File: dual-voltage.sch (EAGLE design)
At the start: 14 parts

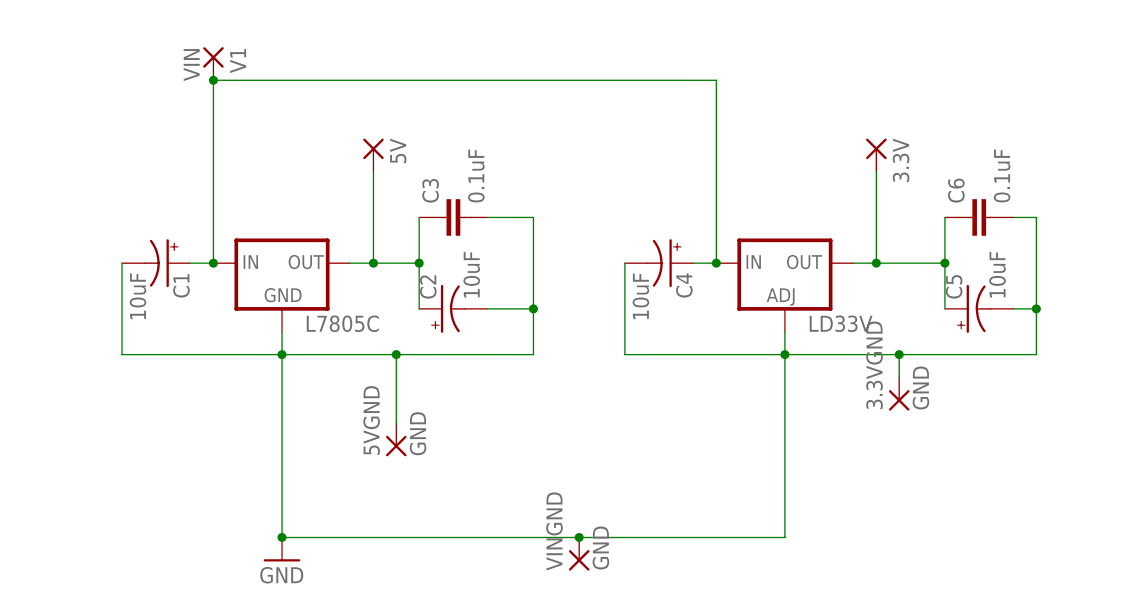
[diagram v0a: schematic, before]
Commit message: Trace updates for new 3.3v regulator
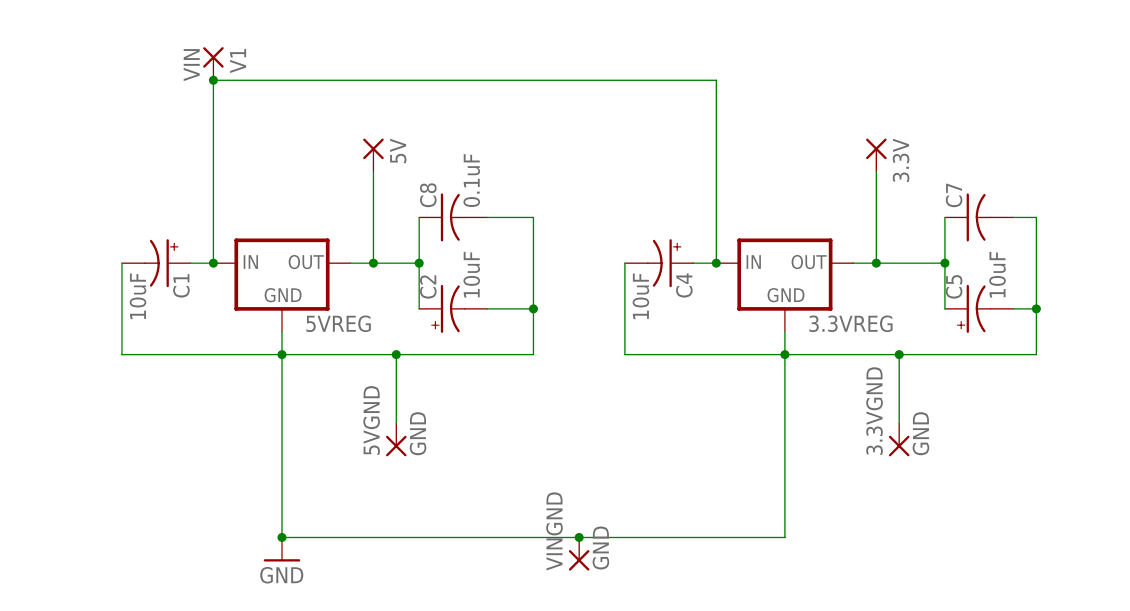
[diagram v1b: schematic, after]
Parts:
- removed C3, C6: 0.1uF, SparkFun-Capacitors:CAPEZ
- removed LD33V: (no value), v-reg:LM317TS
- added 3.3VREG: (no value), v-reg:78XXS
- added C7: (no value), rcl:C-US025-025X050
- added C8: 0.1uF, rcl:C-US025-025X050
- renumbered L7805C to 5VREG
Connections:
- net 3.3V: now also 3.3VREG.OUT, C7.1; no longer C6.1, LD33V.OUT
- net 5V: now also C8.1; no longer C3.1
- net GND: now also 3.3VREG.GND, C7.2, C8.2; no longer C3.2, C6.2, LD33V.ADJ
- net N$1: now also 3.3VREG.IN; no longer LD33V.IN
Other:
- moved on the sheet: 3.3VGND
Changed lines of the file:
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@@
 <part name="C5" library="SparkFun-Capacitors" deviceset="CAP_POL" device="PTH2" value="10uF"/>
 <part name="C4" library="SparkFun-Capacitors" deviceset="CAP_POL" device="PTH2" value="10uF"/>
-<part name="C3" library="SparkFun-Capacitors" deviceset="CAP" device="EZ" value="0.1uF"/>
-<part name="C6" library="SparkFun-Capacitors" deviceset="CAP" device="EZ" value="0.1uF"/>
-<part name="LD33V" library="v-reg" deviceset="LM317TS" device=""/>
-<part name="L7805C" library="v-reg" deviceset="78XXS" device=""/>
+<part name="5VREG" library="v-reg" deviceset="78XXS" device=""/>
 <part name="5V" library="wirepad" deviceset="1,6/0,8" device=""/>
 <part name="3.3V" library="wirepad" deviceset="1,6/0,8" device=""/>
@@
 <part name="VINGND" library="wirepad" deviceset="1,6/0,8" device="" value="GND"/>
 <part name="GND1" library="supply1" deviceset="GND" device=""/>
+<part name="3.3VREG" library="v-reg" deviceset="78XXS" device=""/>
+<part name="C7" library="rcl" deviceset="C-US" device="025-025X050"/>
+<part name="C8" library="rcl" deviceset="C-US" device="025-025X050" value="0.1uF"/>
 </parts>
 <sheets>
@@
 <instance part="C5" gate="G$1" x="109.22" y="53.34" rot="R90"/>
 <instance part="C4" gate="G$1" x="76.2" y="58.42" rot="R270"/>
-<instance part="C3" gate="G$1" x="53.34" y="63.5" rot="R90"/>
-<instance part="C6" gate="G$1" x="111.76" y="63.5" rot="R90"/>
-<instance part="LD33V" gate="1" x="88.9" y="58.42"/>
-<instance part="L7805C" gate="1" x="33.02" y="58.42"/>
+<instance part="5VREG" gate="1" x="33.02" y="58.42"/>
 <instance part="5V" gate="P" x="43.18" y="71.12" rot="R270"/>
 <instance part="3.3V" gate="P" x="99.06" y="71.12" rot="R270"/>
-<instance part="3.3VGND" gate="P" x="101.6" y="43.18" rot="R90"/>
+<instance part="3.3VGND" gate="P" x="101.6" y="38.1" rot="R90"/>
 <instance part="5VGND" gate="P" x="45.72" y="38.1" rot="R90"/>
 <instance part="V1" gate="P" x="25.4" y="81.28" rot="R270"/>
 <instance part="VINGND" gate="P" x="66.04" y="25.4" rot="R90"/>
 <instance part="GND1" gate="1" x="33.02" y="25.4"/>
+<instance part="3.3VREG" gate="1" x="88.9" y="58.42"/>
+<instance part="C7" gate="G$1" x="109.22" y="63.5" rot="R90"/>
+<instance part="C8" gate="G$1" x="50.8" y="63.5" rot="R90"/>
 </instances>
 <busses>
@@
 <net name="5V" class="0">
 <segment>
-<pinref part="C3" gate="G$1" pin="1"/>
 <wire x1="40.64" y1="58.42" x2="43.18" y2="58.42" width="0.1524" layer="91"/>
 <wire x1="43.18" y1="58.42" x2="48.26" y2="58.42" width="0.1524" layer="91"/>
@@
 <wire x1="48.26" y1="53.34" x2="48.26" y2="58.42" width="0.1524" layer="91"/>
 <junction x="48.26" y="58.42"/>
-<pinref part="L7805C" gate="1" pin="OUT"/>
+<pinref part="5VREG" gate="1" pin="OUT"/>
 <pinref part="5V" gate="P" pin="P"/>
 <wire x1="43.18" y1="68.58" x2="43.18" y2="58.42" width="0.1524" layer="91"/>
 <junction x="43.18" y="58.42"/>
+<pinref part="C8" gate="G$1" pin="1"/>
 </segment>
 </net>
 <net name="3.3V" class="0">
 <segment>
-<pinref part="C6" gate="G$1" pin="1"/>
 <wire x1="96.52" y1="58.42" x2="99.06" y2="58.42" width="0.1524" layer="91"/>
 <wire x1="99.06" y1="58.42" x2="106.68" y2="58.42" width="0.1524" layer="91"/>
@@
 <junction x="106.68" y="58.42"/>
 <junction x="99.06" y="58.42"/>
-<pinref part="LD33V" gate="1" pin="OUT"/>
 <pinref part="3.3V" gate="P" pin="P"/>
 <wire x1="99.06" y1="68.58" x2="99.06" y2="58.42" width="0.1524" layer="91"/>
+<pinref part="3.3VREG" gate="1" pin="OUT"/>
+<pinref part="C7" gate="G$1" pin="1"/>
 </segment>
 </net>
@@
 <wire x1="22.86" y1="58.42" x2="25.4" y2="58.42" width="0.1524" layer="91"/>
 <wire x1="25.4" y1="78.74" x2="25.4" y2="58.42" width="0.1524" layer="91"/>
-<pinref part="L7805C" gate="1" pin="IN"/>
+<pinref part="5VREG" gate="1" pin="IN"/>
 <junction x="25.4" y="58.42"/>
 <pinref part="V1" gate="P" pin="P"/>
 <pinref part="C4" gate="G$1" pin="+"/>
 <wire x1="78.74" y1="58.42" x2="81.28" y2="58.42" width="0.1524" layer="91"/>
-<pinref part="LD33V" gate="1" pin="IN"/>
 <wire x1="25.4" y1="78.74" x2="81.28" y2="78.74" width="0.1524" layer="91"/>
 <wire x1="81.28" y1="78.74" x2="81.28" y2="58.42" width="0.1524" layer="91"/>
 <junction x="25.4" y="78.74"/>
+<pinref part="3.3VREG" gate="1" pin="IN"/>
 <junction x="81.28" y="58.42"/>
 </segment>
@@
 <wire x1="60.96" y1="53.34" x2="60.96" y2="48.26" width="0.1524" layer="91"/>
 <wire x1="60.96" y1="48.26" x2="45.72" y2="48.26" width="0.1524" layer="91"/>
-<pinref part="C3" gate="G$1" pin="2"/>
 <wire x1="55.88" y1="63.5" x2="60.96" y2="63.5" width="0.1524" layer="91"/>
 <wire x1="60.96" y1="63.5" x2="60.96" y2="53.34" width="0.1524" layer="91"/>
@@
 <wire x1="71.12" y1="58.42" x2="71.12" y2="48.26" width="0.1524" layer="91"/>
 <wire x1="71.12" y1="48.26" x2="88.9" y2="48.26" width="0.1524" layer="91"/>
-<pinref part="C6" gate="G$1" pin="2"/>
 <wire x1="88.9" y1="48.26" x2="101.6" y2="48.26" width="0.1524" layer="91"/>
 <wire x1="114.3" y1="63.5" x2="116.84" y2="63.5" width="0.1524" layer="91"/>
@@
 <junction x="116.84" y="53.34"/>
 <pinref part="3.3VGND" gate="P" pin="P"/>
-<wire x1="101.6" y1="45.72" x2="101.6" y2="48.26" width="0.1524" layer="91"/>
+<wire x1="101.6" y1="40.64" x2="101.6" y2="48.26" width="0.1524" layer="91"/>
 <junction x="101.6" y="48.26"/>
 <wire x1="66.04" y1="27.94" x2="88.9" y2="27.94" width="0.1524" layer="91"/>
@@
 <pinref part="GND1" gate="1" pin="GND"/>
 <junction x="33.02" y="27.94"/>
+<pinref part="C8" gate="G$1" pin="2"/>
+<pinref part="C7" gate="G$1" pin="2"/>
 </segment>
 <segment>
-<pinref part="L7805C" gate="1" pin="GND"/>
+<pinref part="5VREG" gate="1" pin="GND"/>
 <wire x1="33.02" y1="50.8" x2="33.02" y2="48.26" width="0.1524" layer="91"/>
 </segment>
 <segment>
-<pinref part="LD33V" gate="1" pin="ADJ"/>
 <wire x1="88.9" y1="50.8" x2="88.9" y2="48.26" width="0.1524" layer="91"/>
+<pinref part="3.3VREG" gate="1" pin="GND"/>
 </segment>
 </net>

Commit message: Updates voltage in/out jumpers to SparkFun components, updates 0.1uF capacitor footprint to SparkFun, bumps version to 1.1.0
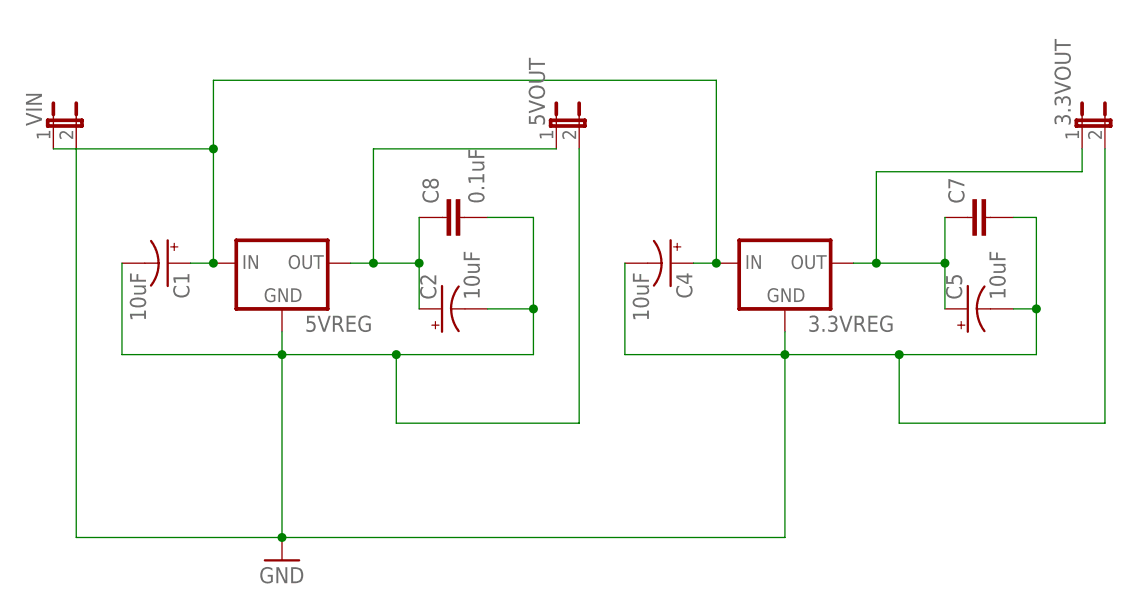
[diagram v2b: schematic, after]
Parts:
- removed 3.3V, 5V: (no value), wirepad:1,6/0,8
- removed 3.3VGND, 5VGND, VINGND: GND, wirepad:1,6/0,8
- removed V1: VIN, wirepad:1,6/0,8
- added 3.3VOUT, 5VOUT, VIN: (no value), SparkFun-Passives:JUMPER-2PTH
- C7, C8: device rcl:C-US025-025X050 -> SparkFun-Passives:CAPPTH2
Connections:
- net 3.3V: now also 3.3VOUT.1; no longer 3.3V.P
- net 5V: now also 5VOUT.1; no longer 5V.P
- net GND: now also 3.3VOUT.2, 5VOUT.2, VIN.2; no longer 3.3VGND.P, 5VGND.P, VINGND.P
- net N$1: now also VIN.1; no longer V1.P
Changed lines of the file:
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@@
 <part name="C4" library="SparkFun-Capacitors" deviceset="CAP_POL" device="PTH2" value="10uF"/>
 <part name="5VREG" library="v-reg" deviceset="78XXS" device=""/>
-<part name="5V" library="wirepad" deviceset="1,6/0,8" device=""/>
-<part name="3.3V" library="wirepad" deviceset="1,6/0,8" device=""/>
-<part name="3.3VGND" library="wirepad" deviceset="1,6/0,8" device="" value="GND"/>
-<part name="5VGND" library="wirepad" deviceset="1,6/0,8" device="" value="GND"/>
-<part name="V1" library="wirepad" deviceset="1,6/0,8" device="" value="VIN"/>
-<part name="VINGND" library="wirepad" deviceset="1,6/0,8" device="" value="GND"/>
 <part name="GND1" library="supply1" deviceset="GND" device=""/>
 <part name="3.3VREG" library="v-reg" deviceset="78XXS" device=""/>
-<part name="C7" library="rcl" deviceset="C-US" device="025-025X050"/>
-<part name="C8" library="rcl" deviceset="C-US" device="025-025X050" value="0.1uF"/>
+<part name="C7" library="SparkFun-Passives" deviceset="CAP" device="PTH2"/>
+<part name="C8" library="SparkFun-Passives" deviceset="CAP" device="PTH2" value="0.1uF"/>
+<part name="5VOUT" library="SparkFun-Passives" deviceset="JUMPER-2" device="PTH"/>
+<part name="3.3VOUT" library="SparkFun-Passives" deviceset="JUMPER-2" device="PTH"/>
+<part name="VIN" library="SparkFun-Passives" deviceset="JUMPER-2" device="PTH"/>
 </parts>
 <sheets>
@@
 <instance part="C4" gate="G$1" x="76.2" y="58.42" rot="R270"/>
 <instance part="5VREG" gate="1" x="33.02" y="58.42"/>
-<instance part="5V" gate="P" x="43.18" y="71.12" rot="R270"/>
-<instance part="3.3V" gate="P" x="99.06" y="71.12" rot="R270"/>
-<instance part="3.3VGND" gate="P" x="101.6" y="38.1" rot="R90"/>
-<instance part="5VGND" gate="P" x="45.72" y="38.1" rot="R90"/>
-<instance part="V1" gate="P" x="25.4" y="81.28" rot="R270"/>
-<instance part="VINGND" gate="P" x="66.04" y="25.4" rot="R90"/>
 <instance part="GND1" gate="1" x="33.02" y="25.4"/>
 <instance part="3.3VREG" gate="1" x="88.9" y="58.42"/>
-<instance part="C7" gate="G$1" x="109.22" y="63.5" rot="R90"/>
-<instance part="C8" gate="G$1" x="50.8" y="63.5" rot="R90"/>
+<instance part="C7" gate="G$1" x="111.76" y="63.5" rot="R90"/>
+<instance part="C8" gate="G$1" x="53.34" y="63.5" rot="R90"/>
+<instance part="5VOUT" gate="A" x="63.5" y="73.66"/>
+<instance part="3.3VOUT" gate="A" x="121.92" y="73.66"/>
+<instance part="VIN" gate="A" x="7.62" y="73.66"/>
 </instances>
 <busses>
@@
 <junction x="48.26" y="58.42"/>
 <pinref part="5VREG" gate="1" pin="OUT"/>
-<pinref part="5V" gate="P" pin="P"/>
-<wire x1="43.18" y1="68.58" x2="43.18" y2="58.42" width="0.1524" layer="91"/>
+<wire x1="43.18" y1="71.12" x2="43.18" y2="58.42" width="0.1524" layer="91"/>
 <junction x="43.18" y="58.42"/>
 <pinref part="C8" gate="G$1" pin="1"/>
+<pinref part="5VOUT" gate="A" pin="1"/>
+<wire x1="63.5" y1="71.12" x2="43.18" y2="71.12" width="0.1524" layer="91"/>
 </segment>
 </net>
@@
 <junction x="106.68" y="58.42"/>
 <junction x="99.06" y="58.42"/>
-<pinref part="3.3V" gate="P" pin="P"/>
 <wire x1="99.06" y1="68.58" x2="99.06" y2="58.42" width="0.1524" layer="91"/>
 <pinref part="3.3VREG" gate="1" pin="OUT"/>
 <pinref part="C7" gate="G$1" pin="1"/>
+<pinref part="3.3VOUT" gate="A" pin="1"/>
+<wire x1="99.06" y1="68.58" x2="121.92" y2="68.58" width="0.1524" layer="91"/>
+<wire x1="121.92" y1="68.58" x2="121.92" y2="71.12" width="0.1524" layer="91"/>
 </segment>
 </net>
@@
 <pinref part="C1" gate="G$1" pin="+"/>
 <wire x1="22.86" y1="58.42" x2="25.4" y2="58.42" width="0.1524" layer="91"/>
-<wire x1="25.4" y1="78.74" x2="25.4" y2="58.42" width="0.1524" layer="91"/>
+<wire x1="25.4" y1="78.74" x2="25.4" y2="71.12" width="0.1524" layer="91"/>
 <pinref part="5VREG" gate="1" pin="IN"/>
 <junction x="25.4" y="58.42"/>
-<pinref part="V1" gate="P" pin="P"/>
 <pinref part="C4" gate="G$1" pin="+"/>
+<wire x1="25.4" y1="71.12" x2="25.4" y2="58.42" width="0.1524" layer="91"/>
 <wire x1="78.74" y1="58.42" x2="81.28" y2="58.42" width="0.1524" layer="91"/>
 <wire x1="25.4" y1="78.74" x2="81.28" y2="78.74" width="0.1524" layer="91"/>
 <wire x1="81.28" y1="78.74" x2="81.28" y2="58.42" width="0.1524" layer="91"/>
-<junction x="25.4" y="78.74"/>
 <pinref part="3.3VREG" gate="1" pin="IN"/>
 <junction x="81.28" y="58.42"/>
+<pinref part="VIN" gate="A" pin="1"/>
+<wire x1="7.62" y1="71.12" x2="25.4" y2="71.12" width="0.1524" layer="91"/>
+<junction x="25.4" y="71.12"/>
 </segment>
 </net>
@@
 <wire x1="60.96" y1="63.5" x2="60.96" y2="53.34" width="0.1524" layer="91"/>
 <junction x="60.96" y="53.34"/>
-<pinref part="5VGND" gate="P" pin="P"/>
 <wire x1="45.72" y1="40.64" x2="45.72" y2="48.26" width="0.1524" layer="91"/>
 <junction x="45.72" y="48.26"/>
-<pinref part="VINGND" gate="P" pin="P"/>
-<wire x1="66.04" y1="27.94" x2="33.02" y2="27.94" width="0.1524" layer="91"/>
+<wire x1="88.9" y1="27.94" x2="33.02" y2="27.94" width="0.1524" layer="91"/>
 <wire x1="33.02" y1="27.94" x2="33.02" y2="48.26" width="0.1524" layer="91"/>
 <junction x="33.02" y="48.26"/>
@@
 <wire x1="114.3" y1="53.34" x2="116.84" y2="53.34" width="0.1524" layer="91"/>
 <junction x="116.84" y="53.34"/>
-<pinref part="3.3VGND" gate="P" pin="P"/>
 <wire x1="101.6" y1="40.64" x2="101.6" y2="48.26" width="0.1524" layer="91"/>
 <junction x="101.6" y="48.26"/>
-<wire x1="66.04" y1="27.94" x2="88.9" y2="27.94" width="0.1524" layer="91"/>
 <wire x1="88.9" y1="27.94" x2="88.9" y2="48.26" width="0.1524" layer="91"/>
-<junction x="66.04" y="27.94"/>
 <junction x="88.9" y="48.26"/>
 <pinref part="GND1" gate="1" pin="GND"/>
@@
 <pinref part="C8" gate="G$1" pin="2"/>
 <pinref part="C7" gate="G$1" pin="2"/>
+<pinref part="5VOUT" gate="A" pin="2"/>
+<wire x1="45.72" y1="40.64" x2="66.04" y2="40.64" width="0.1524" layer="91"/>
+<wire x1="66.04" y1="40.64" x2="66.04" y2="71.12" width="0.1524" layer="91"/>
+<pinref part="3.3VOUT" gate="A" pin="2"/>
+<wire x1="101.6" y1="40.64" x2="124.46" y2="40.64" width="0.1524" layer="91"/>
+<wire x1="124.46" y1="40.64" x2="124.46" y2="71.12" width="0.1524" layer="91"/>
+<pinref part="VIN" gate="A" pin="2"/>
+<wire x1="10.16" y1="71.12" x2="10.16" y2="27.94" width="0.1524" layer="91"/>
+<wire x1="10.16" y1="27.94" x2="33.02" y2="27.94" width="0.1524" layer="91"/>
 </segment>
 <segment>
